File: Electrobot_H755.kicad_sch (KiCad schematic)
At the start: 83 parts, among them J1 Conn_XT30M, J10 Conn_01x04, J11 Conn_01x04, J12 Conn_01x04, J13 Conn_01x04, J14 Conn_01x04, J15 Conn_01x03, J16 Conn_01x03, J17 Conn_01x04, J18 Conn_01x03, J19 Conn_01x03, J2 Conn_01x04, J20 Conn_01x03, J21 Conn_01x03, J22 Conn_01x04, J3 Conn_01x04, J4 Conn_01x04, J5 Conn_01x04, J6 Conn_01x04, J7 Conn_01x04, J8 Conn_01x04, J9 Conn_01x04, U2 TSR_2-2450, U3 TSR_2-2465, U4 TSR_2-2465

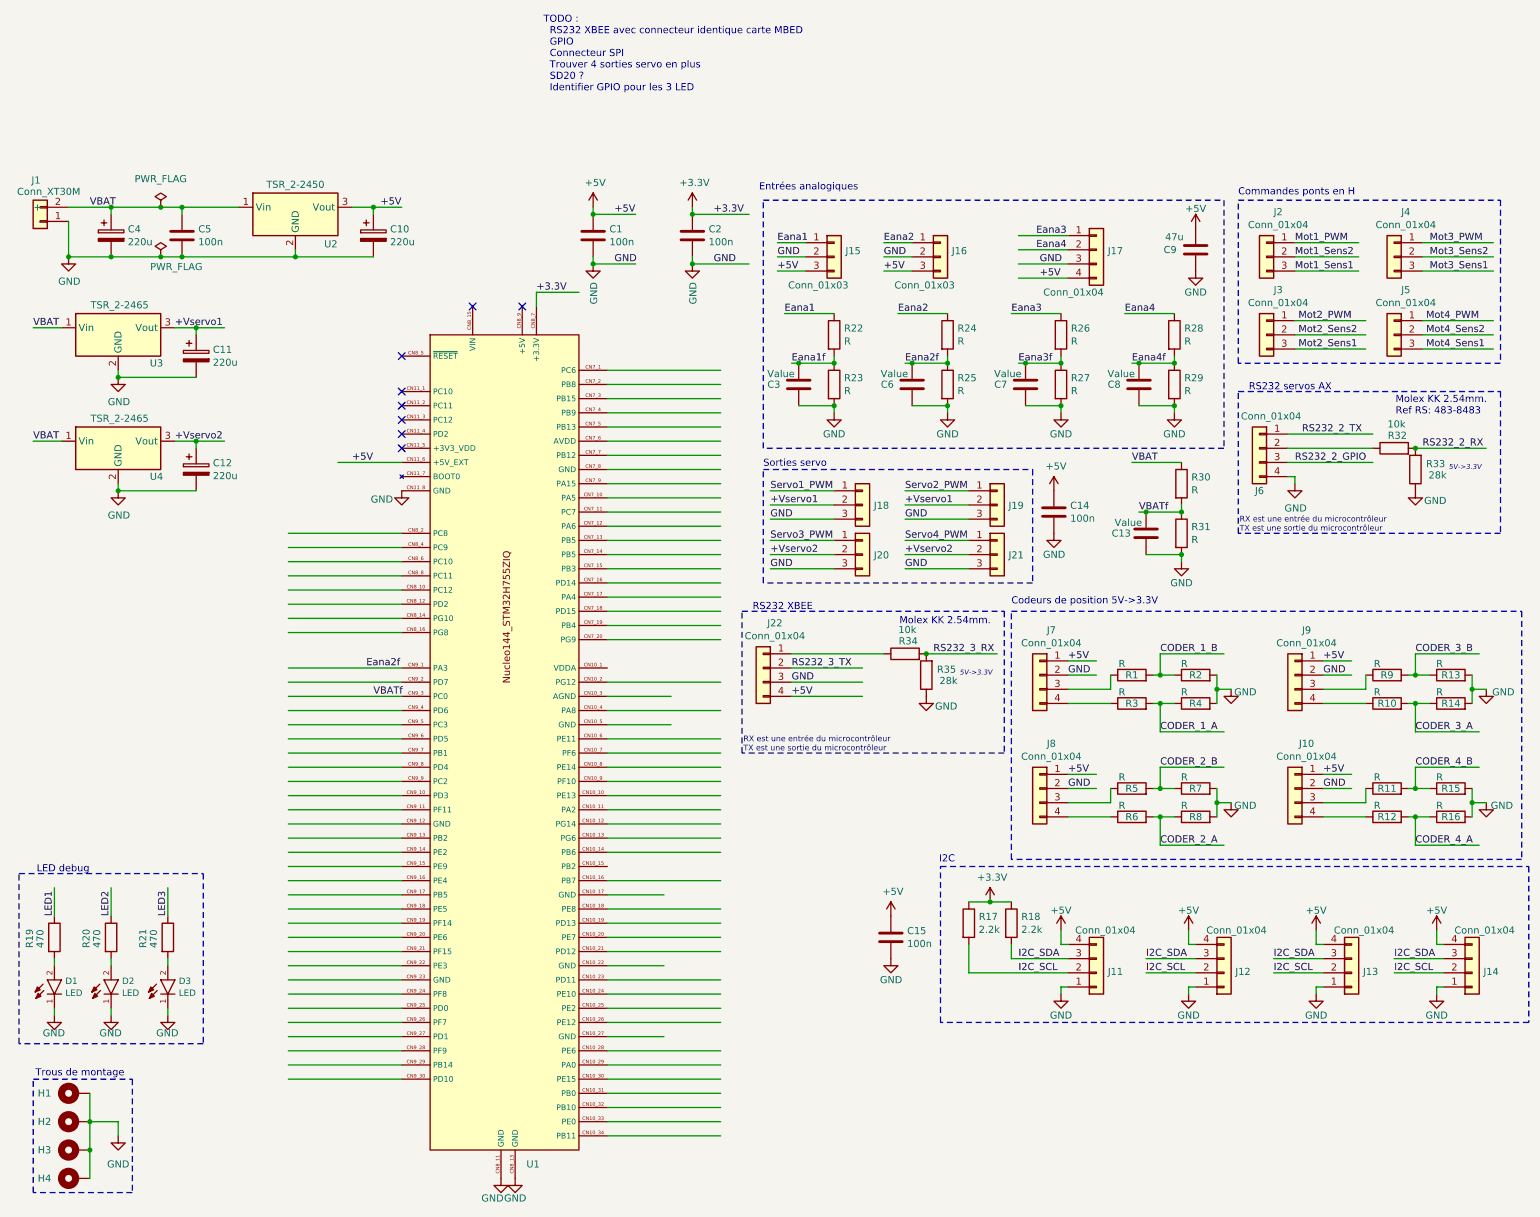
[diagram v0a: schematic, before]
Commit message: Mise à jour du schéma
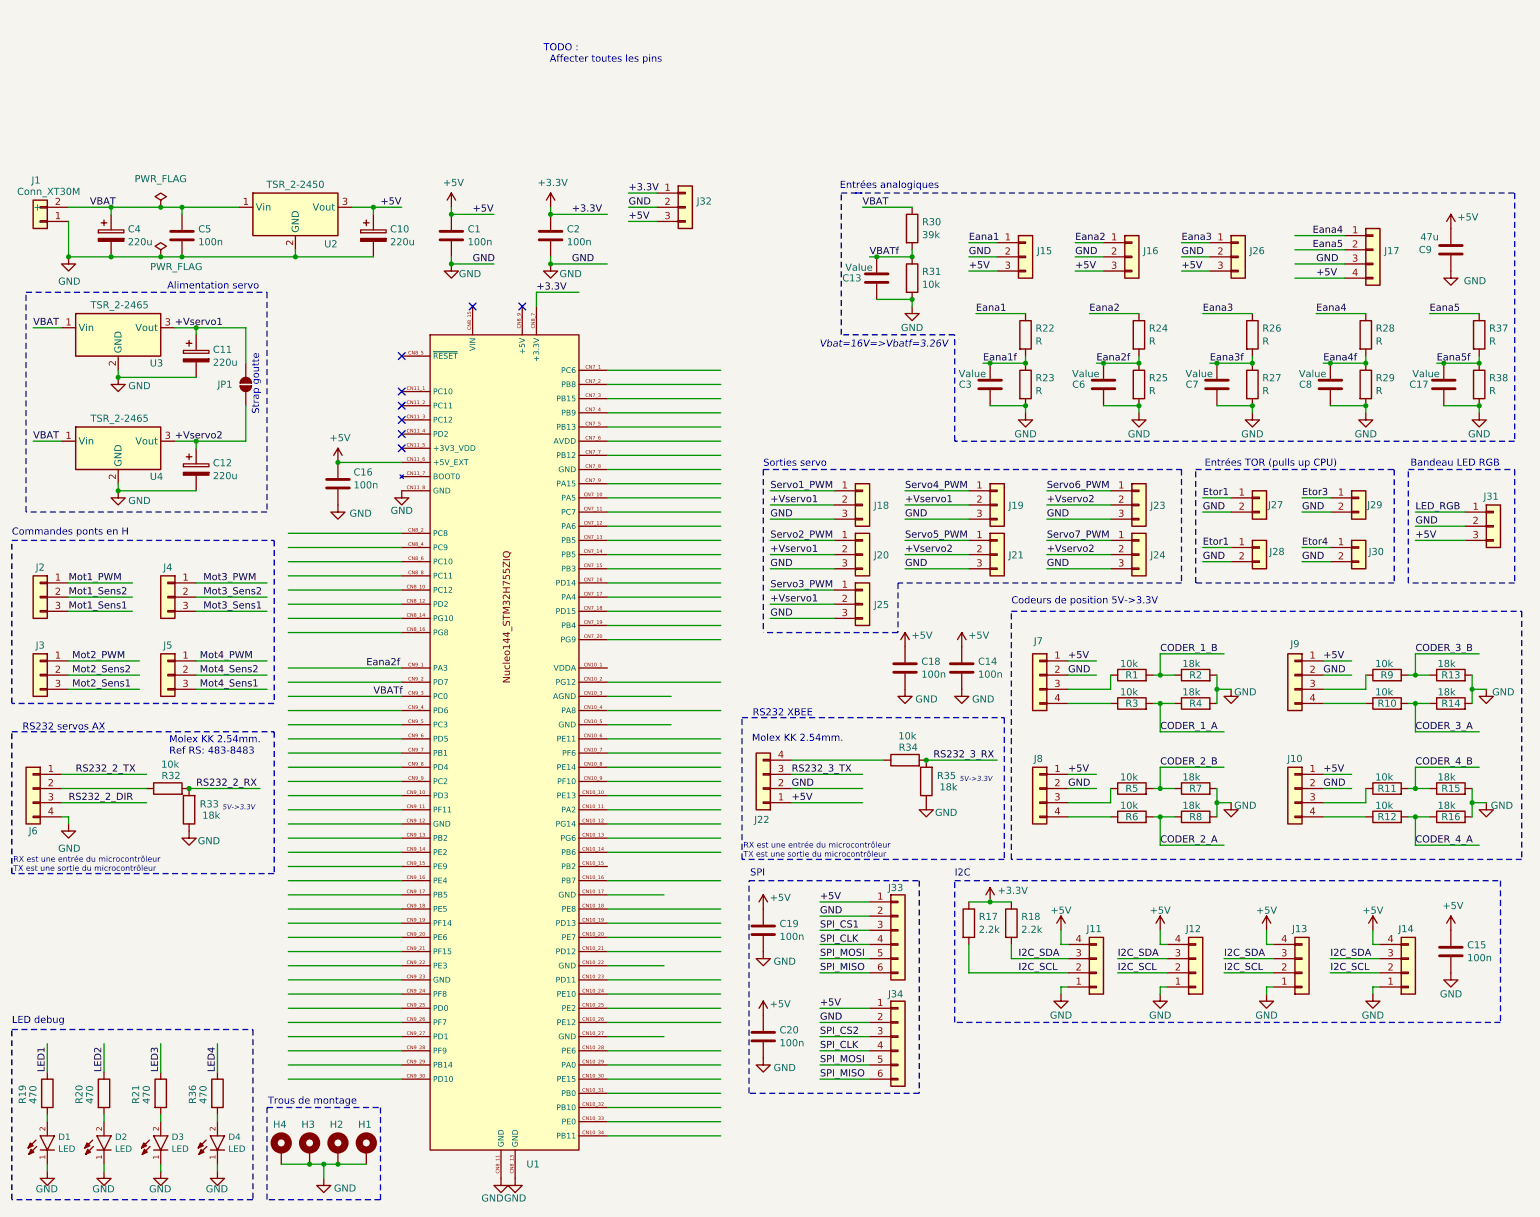
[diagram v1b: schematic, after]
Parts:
- added C16, C18, C19, C20: 100n, Capacitor_SMD:C_1206_3216Metric, symbol CRLG-Passive:C
- added C17: Value, Capacitor_SMD:C_1206_3216Metric, symbol CRLG-Passive:C
- added D4: LED, LED_SMD:LED_1206_3216Metric, symbol CRLG-Passive:LED
- added J23, J24, J25: Conn_01x03, Servomotors:Servomotor-3x254, symbol CRLG-Connectors:Conn_01x03
- added J26, J31, J32: Conn_01x03, Connector_Molex:Molex_KK-254_AE-6410-03A_1x03_P2.54mm_Vertical, symbol CRLG-Connectors:Conn_01x03
- added J27, J28, J29, J30: Conn_01x02, Connector_Molex:Molex_KK-254_AE-6410-02A_1x02_P2.54mm_Vertical, symbol CRLG-Connectors:Conn_01x02
- added J33, J34: Conn_01x06, Connector_Molex:Molex_KK-254_AE-6410-06A_1x06_P2.54mm_Vertical, symbol CRLG-Connectors:Conn_01x06
- added JP1: SolderJumper_2_Open, Jumper:SolderJumper-2_P1.3mm_Open_TrianglePad1.0x1.5mm, symbol Jumper:SolderJumper_2_Open
- added R36: 470, Resistor_SMD:R_1206_3216Metric, symbol CRLG-Passive:R
- added R37, R38: R, Resistor_SMD:R_1206_3216Metric, symbol CRLG-Passive:R
- R1, R10, R11, R12, R3, R5, R6, R9: value R -> 10k; footprint (none) -> Resistor_SMD:R_1206_3216Metric
- R13, R14, R15, R16, R2, R4, R7, R8: value R -> 18k; footprint (none) -> Resistor_SMD:R_1206_3216Metric
- R30: value R -> 39k
- R31: value R -> 10k
- R33, R35: value 28k -> 18k
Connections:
- net +3.3V: now also J32.1 (Pin_1)
- net +5V: now also J22.1 (Pin_1), C16.1, C18.1, C19.1, C20.1, J26.3 (Pin_3), J31.3 (Pin_3), J32.3 (Pin_3), J33.1 (Pin_1), J34.1 (Pin_1); no longer J22.4 (Pin_4)
- net +Vservo1: now also J20.2 (Pin_2), J25.2 (Pin_2), JP1.2 (B)
- net +Vservo2: now also J23.2 (Pin_2), J24.2 (Pin_2), JP1.1 (A); no longer J20.2 (Pin_2)
- net Eana3: now also J26.1 (Pin_1); no longer J17.1 (Pin_1)
- net Eana4: now also J17.1 (Pin_1); no longer J17.2 (Pin_2)
- net GND: now also J22.2 (Pin_2), C16.2, C17.1, C18.2, C19.2, C20.2, D4.1 (C), J23.3 (Pin_3), J24.3 (Pin_3), J25.3 (Pin_3), J26.2 (Pin_2), J27.2 (Pin_2), J28.2 (Pin_2), J29.2 (Pin_2), J30.2 (Pin_2), J31.2 (Pin_2), J32.2 (Pin_2), J33.2 (Pin_2), J34.2 (Pin_2), R38.2; no longer J22.3 (Pin_3)
- net RS232_3_TX: now also J22.3 (Pin_3); no longer J22.2 (Pin_2)
- net Servo2_PWM: now also J20.1 (Pin_1); no longer J19.1 (Pin_1)
- net Servo3_PWM: now also J25.1 (Pin_1); no longer J20.1 (Pin_1)
- net Servo4_PWM: now also J19.1 (Pin_1); no longer J21.1 (Pin_1)
- net at R34.1: now also J22.4 (Pin_4); no longer J22.1 (Pin_1)
- net RS232_2_GPIO renamed RS232_2_DIR
- new net: D4.2 (A), R36.2
- new net Eana5: J17.2 (Pin_2), R37.1
- new net Eana5f: C17.2, R37.2, R38.1
- new net Etor1: J27.1 (Pin_1), J28.1 (Pin_1)
- new net Etor3: J29.1 (Pin_1)
- new net Etor4: J30.1 (Pin_1)
- new net LED4: R36.1
- new net LED_RGB: J31.1 (Pin_1)
- new net SPI_CLK: J33.4 (Pin_4), J34.4 (Pin_4)
- new net SPI_CS1: J33.3 (Pin_3)
- new net SPI_CS2: J34.3 (Pin_3)
- new net SPI_MISO: J33.6 (Pin_6), J34.6 (Pin_6)
- new net SPI_MOSI: J33.5 (Pin_5), J34.5 (Pin_5)
- new net Servo5_PWM: J21.1 (Pin_1)
- new net Servo6_PWM: J23.1 (Pin_1)
- new net Servo7_PWM: J24.1 (Pin_1)
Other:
- note added: "Alimentation servo"
- note added: "Bandeau LED RGB"
- note added: "Entrées TOR (pulls up CPU)"
- note added: "SPI"
- note added: "Strap goutte"
- note added: "TODO : Affecter toutes les pins"
- note added: "Vbat=16V=>Vbatf=3.26V"
- note removed: "TODO : RS232 XBEE avec connecteur identique carte MBED GPIO Connecteur SPI Trouver 4 sorties servo en plus SD20 ? Identifier GPIO pour les 3 LED"
- moved on the sheet: C1, C13, C14, C15, C2, C3, C6, C7, C8, C9, D1, D2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

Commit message: Mise à jour du schéma
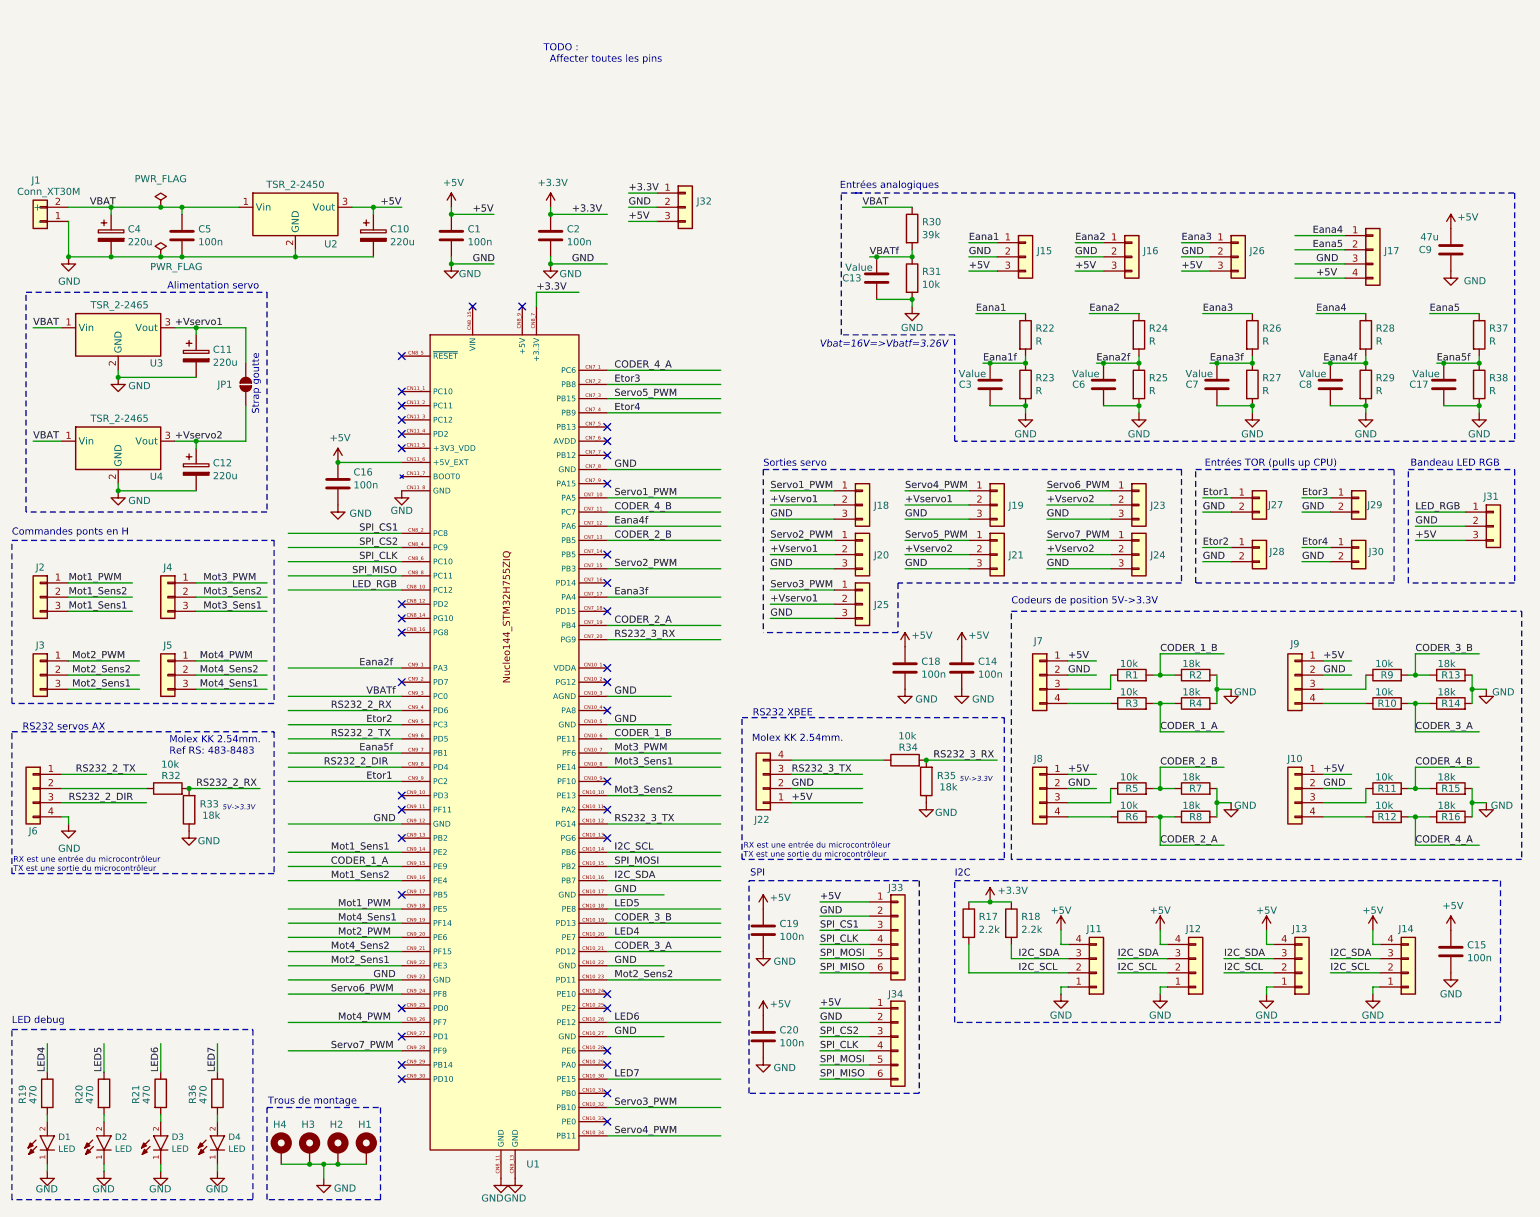
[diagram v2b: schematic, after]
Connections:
- net LED1 is gone; now on net LED4: R19.1
- net LED2 is gone; now on net LED5: R20.1
- net LED3 is gone; now on net LED6: R21.1
- net CODER_1_A: now also U1.CN9_15 (PE9)
- net CODER_1_B: now also U1.CN10_6 (PE11)
- net CODER_2_A: now also U1.CN7_19 (PB4)
- net CODER_2_B: now also U1.CN7_13 (PB5)
- net CODER_3_A: now also U1.CN10_21 (PD12)
- net CODER_3_B: now also U1.CN10_19 (PD13)
- net CODER_4_A: now also U1.CN7_1 (PC6)
- net CODER_4_B: now also U1.CN7_11 (PC7)
- net Eana3f: now also U1.CN7_17 (PA4)
- net Eana4f: now also U1.CN7_12 (PA6)
- net Eana5f: now also U1.CN9_7 (PB1)
- net Etor1: now also U1.CN9_9 (PC2); no longer J28.1 (Pin_1)
- net Etor3: now also U1.CN7_2 (PB8)
- net Etor4: now also U1.CN7_4 (PB9)
- net GND: now also U1.CN10_17 (GND), U1.CN10_22 (GND), U1.CN10_27 (GND), U1.CN10_3 (AGND), U1.CN10_5 (GND), U1.CN7_8 (GND), U1.CN9_12 (GND), U1.CN9_23 (GND)
- net I2C_SCL: now also U1.CN10_14 (PB6)
- net I2C_SDA: now also U1.CN10_16 (PB7)
- net LED4: now also U1.CN10_20 (PE7); no longer R36.1
- net LED_RGB: now also U1.CN8_10 (PC12)
- net Mot1_PWM: now also U1.CN9_18 (PE5)
- net Mot1_Sens1: now also U1.CN9_14 (PE2)
- net Mot1_Sens2: now also U1.CN9_16 (PE4)
- net Mot2_PWM: now also U1.CN9_20 (PE6)
- net Mot2_Sens1: now also U1.CN9_22 (PE3)
- net Mot2_Sens2: now also U1.CN10_23 (PD11)
- net Mot3_PWM: now also U1.CN10_7 (PF6)
- net Mot3_Sens1: now also U1.CN10_8 (PE14)
- net Mot3_Sens2: now also U1.CN10_10 (PE13)
- net Mot4_PWM: now also U1.CN9_26 (PF7)
- net Mot4_Sens1: now also U1.CN9_19 (PF14)
- net Mot4_Sens2: now also U1.CN9_21 (PF15)
- net RS232_2_DIR: now also U1.CN9_8 (PD4)
- net RS232_2_RX: now also U1.CN9_4 (PD6)
- net RS232_2_TX: now also U1.CN9_6 (PD5)
- net RS232_3_RX: now also U1.CN7_20 (PG9)
- net RS232_3_TX: now also U1.CN10_12 (PG14)
- net SPI_CLK: now also U1.CN8_6 (PC10)
- net SPI_CS1: now also U1.CN8_2 (PC8)
- net SPI_CS2: now also U1.CN8_4 (PC9)
- net SPI_MISO: now also U1.CN8_8 (PC11)
- net SPI_MOSI: now also U1.CN10_15 (PB2)
- net Servo1_PWM: now also U1.CN7_10 (PA5)
- net Servo2_PWM: now also U1.CN7_15 (PB3)
- net Servo3_PWM: now also U1.CN10_32 (PB10)
- net Servo4_PWM: now also U1.CN10_34 (PB11)
- net Servo5_PWM: now also U1.CN7_3 (PB15)
- net Servo6_PWM: now also U1.CN9_24 (PF8)
- net Servo7_PWM: now also U1.CN9_28 (PF9)
- net LED5: now reaches U1.CN10_18 (PE8)
- net LED6: now reaches U1.CN10_26 (PE12)
- net LED7: now reaches U1.CN10_30 (PE15)
- net LED7: now also R36.1
- net Etor2: now reaches U1.CN9_5 (PC3)
- net Etor2: now also J28.1 (Pin_1)
- no-connect marks 8 -> 39

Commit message: Evolutions/corrections suite à la séance de relecture du 08/01/2025 avec Ben et LaGuiche
- Correction entrée analogique Eana1
- Ajout d'un connecteur de reset déporté
- Ajout d'un 5ème connecteur I2C
- Changement de l'empreinte du jumper Vservo1 - 2
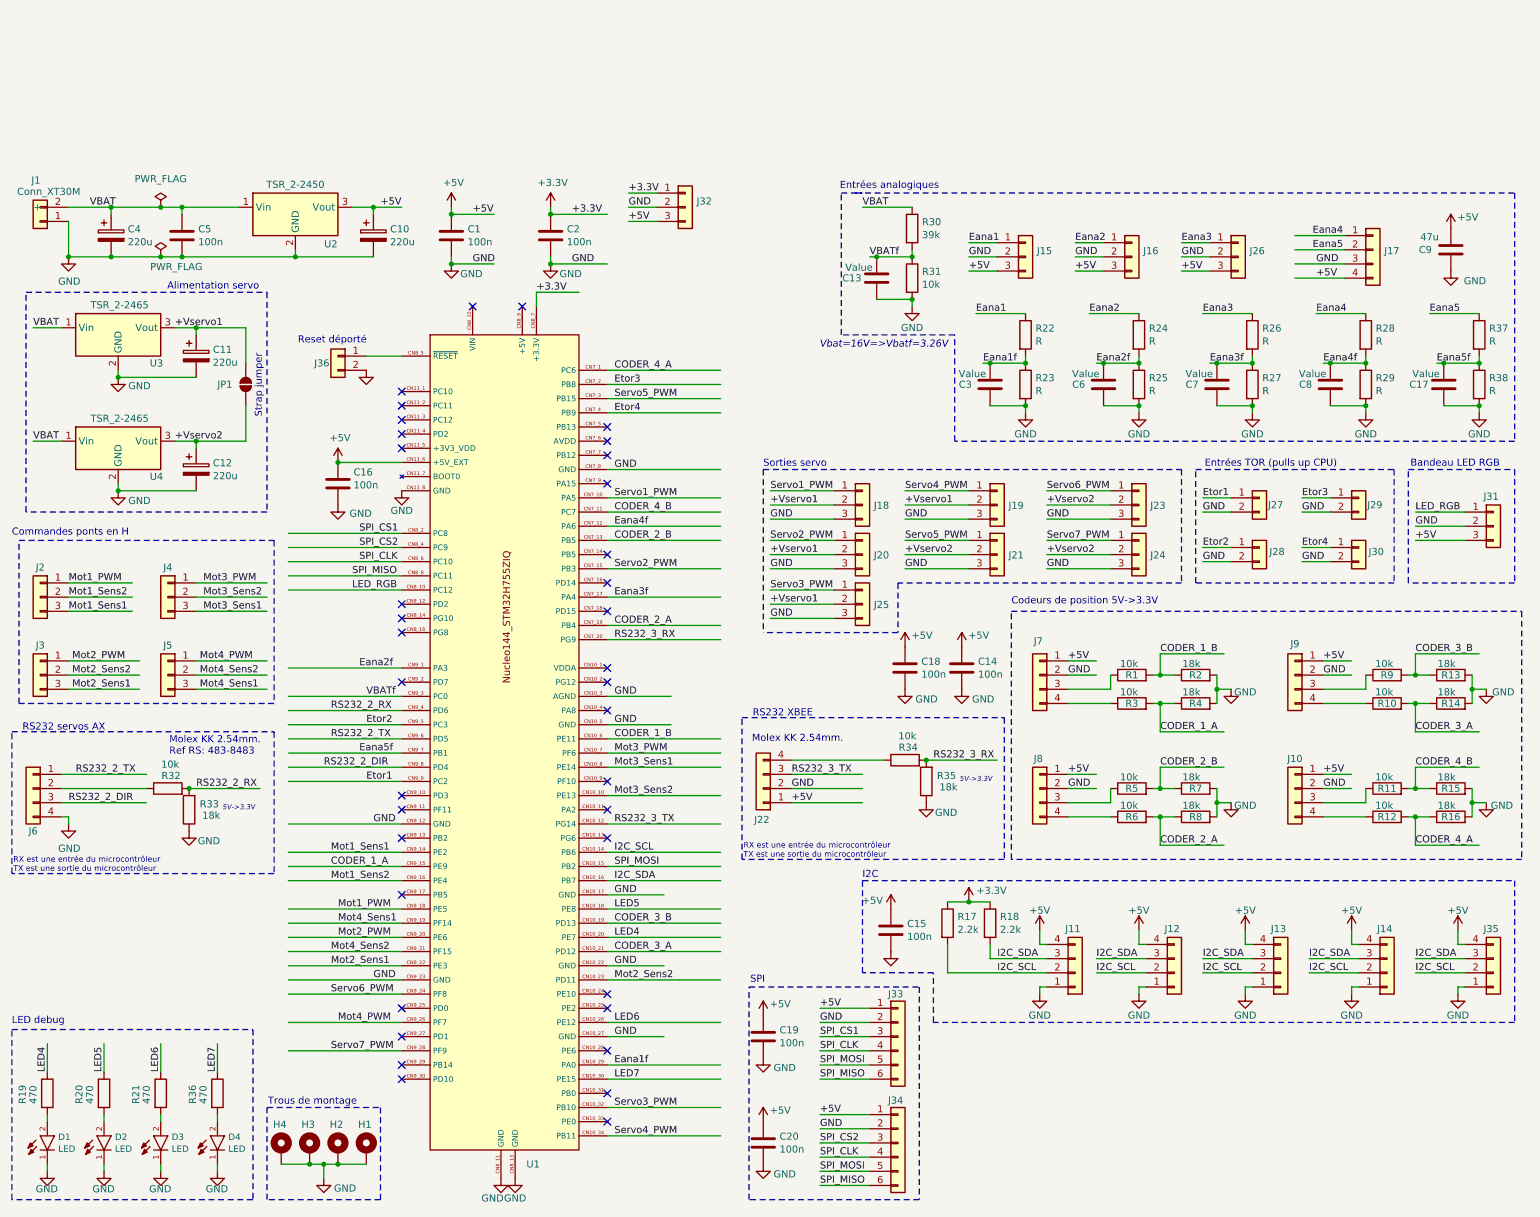
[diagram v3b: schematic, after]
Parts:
- added J35: Conn_01x04, Connector_Molex:Molex_KK-254_AE-6410-04A_1x04_P2.54mm_Vertical, symbol CRLG-Connectors:Conn_01x04
- added J36: Conn_01x02, Connector_Molex:Molex_KK-254_AE-6410-02A_1x02_P2.54mm_Vertical, symbol CRLG-Connectors:Conn_01x02
- JP1: footprint Jumper:SolderJumper-2_P1.3mm_Open_TrianglePad1.0x1.5mm -> Connector_PinHeader_2.54mm:PinHeader_1x02_P2.54mm_Vertical
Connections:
- net +5V: now also J35.4 (Pin_4)
- net Eana1f: now also U1.CN10_29 (PA0)
- net GND: now also J35.1 (Pin_1), J36.2 (Pin_2)
- net I2C_SCL: now also J35.2 (Pin_2)
- net I2C_SDA: now also J35.3 (Pin_3)
- net at U1.CN8_5 (~{RESET}): now also J36.1 (Pin_1)
- no-connect marks 39 -> 37
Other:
- note added: "Reset déporté"
- note added: "Strap jumper"
- note removed: "Strap goutte"
- note removed: "TODO : Affecter toutes les pins"
- moved on the sheet: C15, C19, C20, J11, J12, J13, J14, J33, J34, R17, R18
